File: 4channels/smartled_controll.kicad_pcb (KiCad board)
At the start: 2 copper layers, 61.2 x 43.7 mm, 101 parts, among them J1 Conn_01x04, J2 Conn_01x02, SW1 SW_Push, U1 OC5028B, U2 MAX485E, U3 PY32F003F1xUx, U4 OC5864, U5 SGM2033-3.3, U6 OC5028B, U7 GS8521, U8 OC5028B, U9 OC5028B, Y1 Crystal_GND23

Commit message: 按照OC5028B数据手册，散热焊接与SW引脚连接 修复Out-与In-短路问题，已有PCB在散热焊盘涂阻焊油处理
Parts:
- U1, U6, U8, U9: footprint Package_SO:HSOP-8-1EP_3.9x4.9mm_P1.27mm_EP2.41x3.1mm_ThermalVias -> project_footprints:HSOP-8-1EP_3.9x4.9mm_P1.27mm_EP2.41x3.1mm_ThermalVias_0.3_0.6mm
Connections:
- U1 pad 9: GND -> Net-(D5-A)
- U6 pad 9: GND -> Net-(D9-A)
- U8 pad 9: GND -> Net-(D10-A)
- U9 pad 9: GND -> Net-(D11-A)
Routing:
- net GND: track 306.8 -> 384.1 mm, vias 2 -> 13
- net +5V: track 93.9 -> 99.1 mm
- net Net-(D9-A): track 7.81 -> 9.76 mm
- net Net-(D5-A): track 7.81 -> 9.76 mm
- net Net-(D11-A): track 7.81 -> 9.76 mm
- net Net-(D10-A): track 7.81 -> 9.76 mm

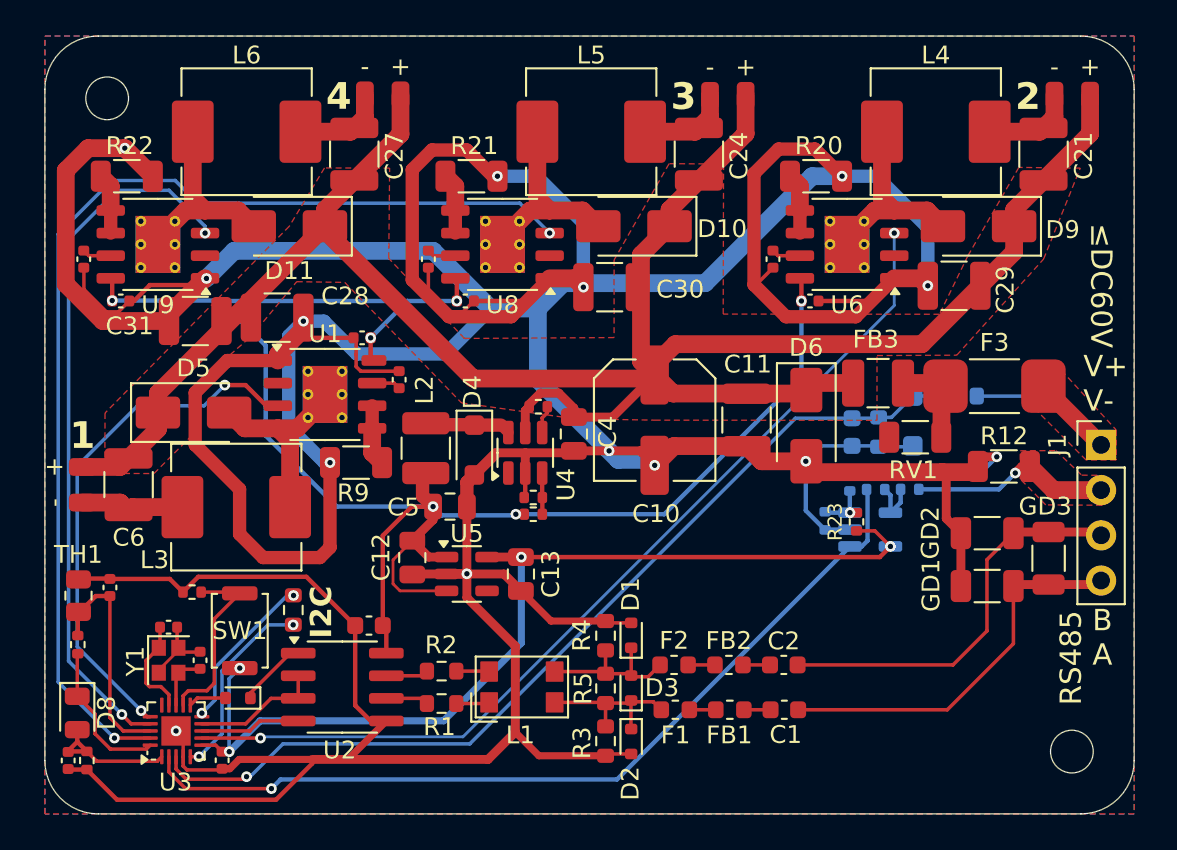
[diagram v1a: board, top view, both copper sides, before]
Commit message: 加宽散热走线
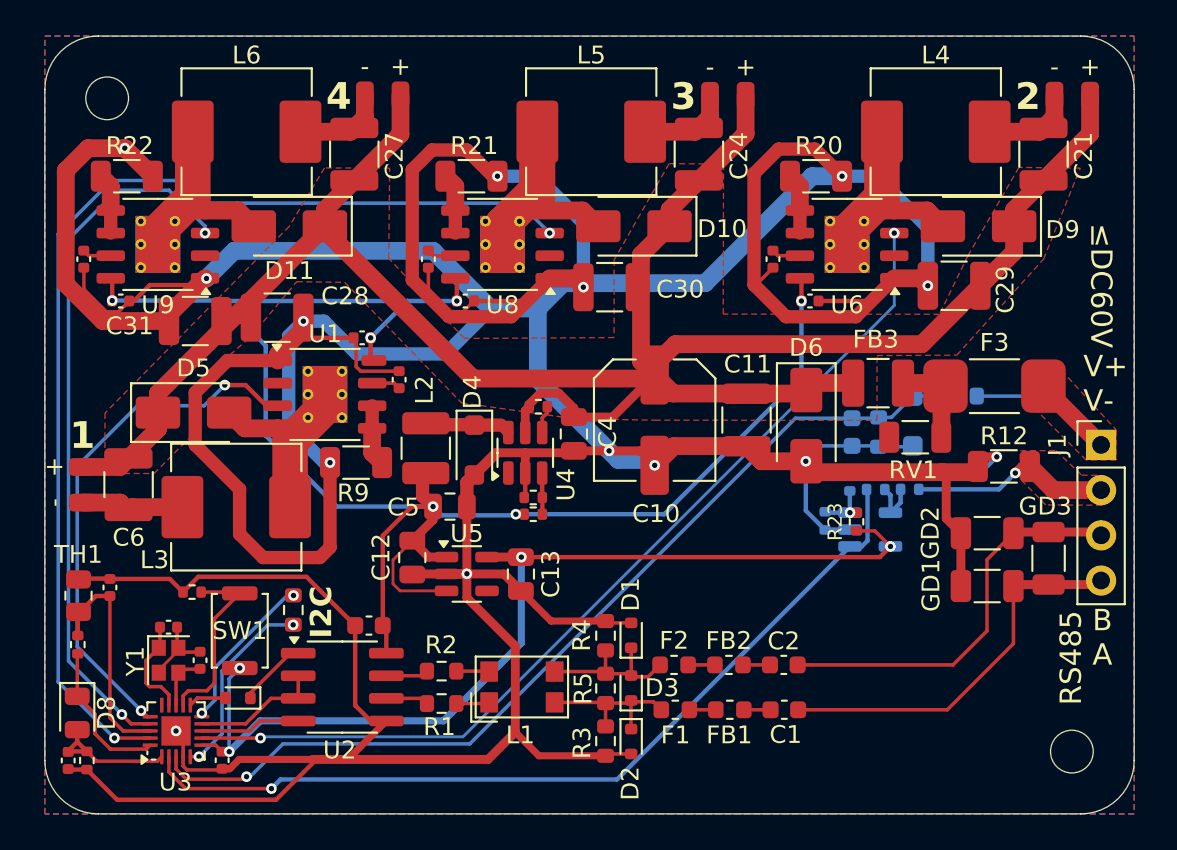
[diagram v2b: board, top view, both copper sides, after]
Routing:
- net Net-(D10-A): track 9.76 -> 15.5 mm
- net Net-(D11-A): track 9.76 -> 12.7 mm
- net Net-(D5-A): track 9.76 -> 12.7 mm
- net Net-(D9-A): track 9.76 -> 12.7 mm
